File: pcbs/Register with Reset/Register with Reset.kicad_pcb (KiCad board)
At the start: 2 copper layers, 101.6 x 114.3 mm, 73 parts, among them J101 Conn_02x20_Odd_Even, U201 74HC245, U202 74HCT574, U203 74HC245, U301 74HC245, U302 74HCT574, U303 74HC245, U401 74HC08, U402 74HC14

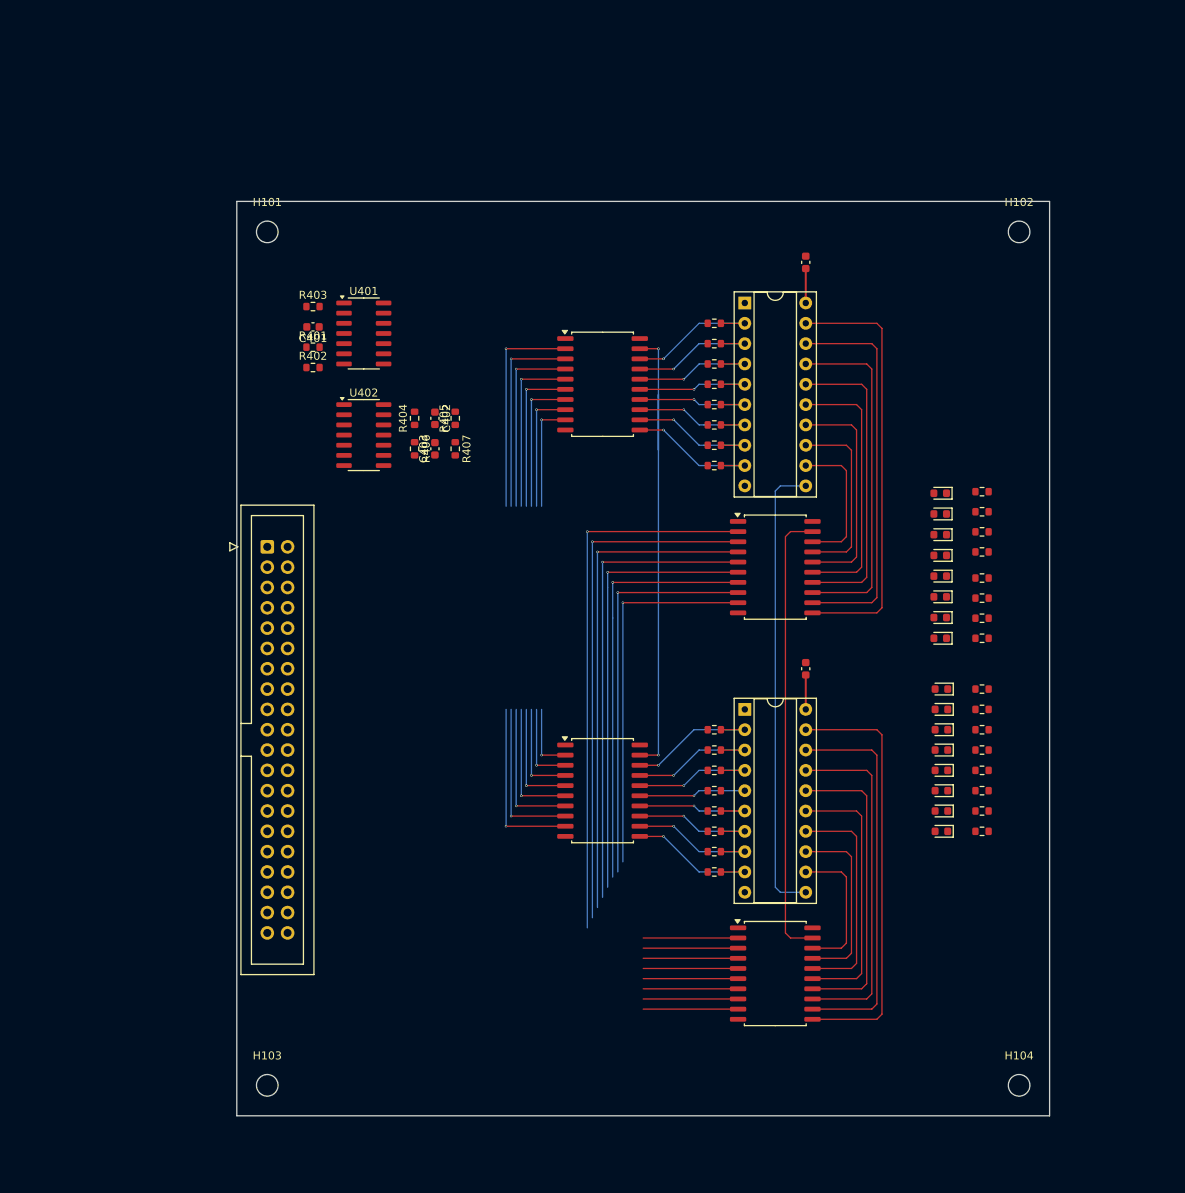
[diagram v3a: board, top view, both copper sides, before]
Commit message: First draft of whole board
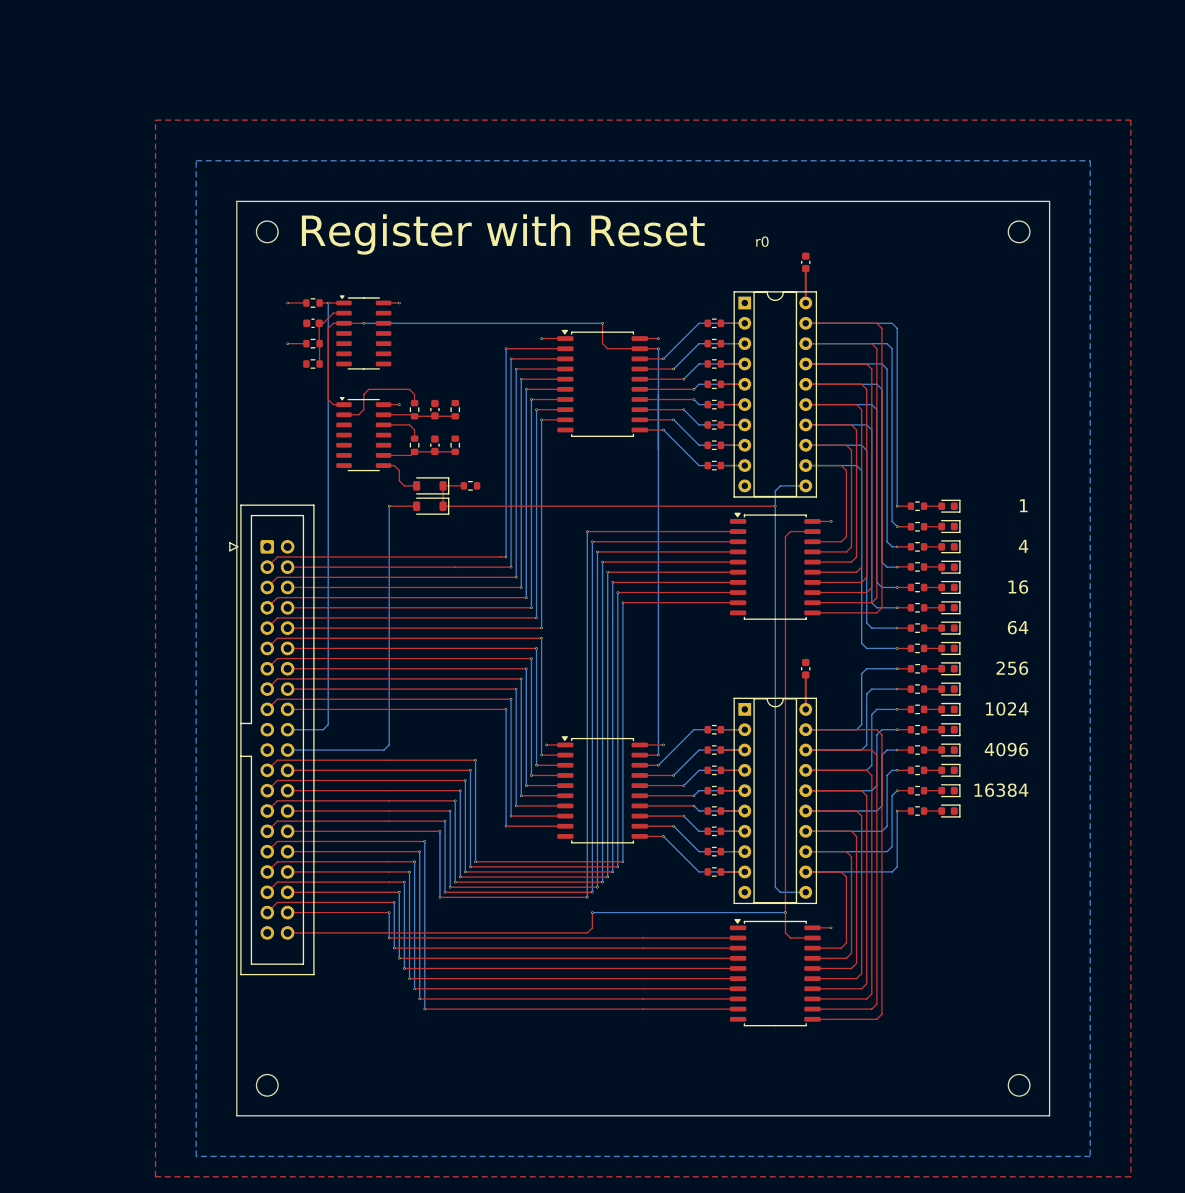
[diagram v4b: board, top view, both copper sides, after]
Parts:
- added D101: D, Diode_SMD:D_SOD-123, F.Cu at (87.6, 99.1)
- added D102: D, Diode_SMD:D_SOD-123, F.Cu at (87.6, 101.6)
- added R101: 1M, Resistor_SMD:R_0603_1608Metric, F.Cu at (92.7, 99.1)
- moved R312 8.46 mm to (148.6, 129.5)
- moved R316 8.46 mm to (148.6, 139.7)
- moved R310 8.46 mm to (148.6, 124.5)
- moved R309 8.46 mm to (148.6, 121.9)
- moved R311 8.46 mm to (148.6, 127.0)
- moved R313 8.46 mm to (148.6, 132.1)
- moved R314 8.46 mm to (148.6, 134.6)
- moved R315 8.46 mm to (148.6, 137.2)
- moved R210 8.28 mm to (148.6, 104.2)
- moved R211 8.28 mm to (148.6, 106.7)
- moved R212 8.28 mm to (148.6, 109.2)
- moved R209 8.27 mm to (148.6, 101.6)
- moved R216 8.16 mm to (148.6, 119.4)
- moved R215 8.16 mm to (148.6, 116.8)
- moved R214 8.16 mm to (148.6, 114.3)
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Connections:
- D201 pad 1: Net-(D201-K) -> GND
- D202 pad 1: Net-(D202-K) -> GND
- D203 pad 1: Net-(D203-K) -> GND
- D204 pad 1: Net-(D204-K) -> GND
- D205 pad 1: Net-(D205-K) -> GND
- D206 pad 1: Net-(D206-K) -> GND
- D207 pad 1: Net-(D207-K) -> GND
- D208 pad 1: Net-(D208-K) -> GND
- D301 pad 1: Net-(D301-K) -> GND
- D302 pad 1: Net-(D302-K) -> GND
- D303 pad 1: Net-(D303-K) -> GND
- D304 pad 1: Net-(D304-K) -> GND
- D305 pad 1: Net-(D305-K) -> GND
- D306 pad 1: Net-(D306-K) -> GND
- D307 pad 1: Net-(D307-K) -> GND
- D308 pad 1: Net-(D308-K) -> GND
- J101 pad 20: unconnected-(J101-Pin_20-Pad20) -> /~{RESET}
- J101 pad 22: unconnected-(J101-Pin_22-Pad22) -> /CLK
- J101 pad 40: unconnected-(J101-Pin_40-Pad40) -> /~{OE}
- R209 pad 1: Net-(D201-K) -> Net-(U202-Q0)
- R209 pad 2: GND -> Net-(D201-A)
- R210 pad 1: Net-(D202-K) -> Net-(U202-Q1)
- R210 pad 2: GND -> Net-(D202-A)
- R211 pad 1: Net-(D203-K) -> Net-(U202-Q2)
- R211 pad 2: GND -> Net-(D203-A)
- R212 pad 1: Net-(D204-K) -> Net-(U202-Q3)
- R212 pad 2: GND -> Net-(D204-A)
- R213 pad 1: Net-(D205-K) -> Net-(U202-Q4)
- R213 pad 2: GND -> Net-(D205-A)
- R214 pad 1: Net-(D206-K) -> Net-(U202-Q5)
- R214 pad 2: GND -> Net-(D206-A)
- R215 pad 1: Net-(D207-K) -> Net-(U202-Q6)
- R215 pad 2: GND -> Net-(D207-A)
- R216 pad 1: Net-(D208-K) -> Net-(U202-Q7)
- R216 pad 2: GND -> Net-(D208-A)
- R309 pad 1: Net-(D301-K) -> Net-(U302-Q0)
- R309 pad 2: GND -> Net-(D301-A)
- R310 pad 1: Net-(D302-K) -> Net-(U302-Q1)
- R310 pad 2: GND -> Net-(D302-A)
- R311 pad 1: Net-(D303-K) -> Net-(U302-Q2)
- R311 pad 2: GND -> Net-(D303-A)
- R312 pad 1: Net-(D304-K) -> Net-(U302-Q3)
- R312 pad 2: GND -> Net-(D304-A)
- R313 pad 1: Net-(D305-K) -> Net-(U302-Q4)
- R313 pad 2: GND -> Net-(D305-A)
- R314 pad 1: Net-(D306-K) -> Net-(U302-Q5)
- R314 pad 2: GND -> Net-(D306-A)
- R315 pad 1: Net-(D307-K) -> Net-(U302-Q6)
- R315 pad 2: GND -> Net-(D307-A)
- R316 pad 1: Net-(D308-K) -> Net-(U302-Q7)
- R316 pad 2: GND -> Net-(D308-A)
- R403 pad 2: /ResetLogic/~{RESET} -> /~{RESET}
- R404 pad 1: Net-(R404-Pad1) -> Net-(C402-Pad1)
- R404 pad 2: Net-(C402-Pad1) -> Net-(R404-Pad2)
- R405 pad 1: GND -> Net-(C402-Pad1)
- R405 pad 2: Net-(C402-Pad1) -> GND
- R406 pad 1: Net-(R406-Pad1) -> Net-(C403-Pad1)
- R406 pad 2: Net-(C403-Pad1) -> Net-(R406-Pad2)
- R407 pad 1: GND -> Net-(C403-Pad1)
- R407 pad 2: Net-(C403-Pad1) -> GND
- U202 pad 12: Net-(D208-A) -> Net-(U202-Q7)
- U202 pad 13: Net-(D207-A) -> Net-(U202-Q6)
- U202 pad 14: Net-(D206-A) -> Net-(U202-Q5)
- U202 pad 15: Net-(D205-A) -> Net-(U202-Q4)
- U202 pad 16: Net-(D204-A) -> Net-(U202-Q3)
- U202 pad 17: Net-(D203-A) -> Net-(U202-Q2)
- U202 pad 18: Net-(D202-A) -> Net-(U202-Q1)
- U202 pad 19: Net-(D201-A) -> Net-(U202-Q0)
- U203 pad 11: Net-(D201-A) -> Net-(U202-Q0)
- U203 pad 12: Net-(D202-A) -> Net-(U202-Q1)
- U203 pad 13: Net-(D203-A) -> Net-(U202-Q2)
- U203 pad 14: Net-(D204-A) -> Net-(U202-Q3)
- U203 pad 15: Net-(D205-A) -> Net-(U202-Q4)
- U203 pad 16: Net-(D206-A) -> Net-(U202-Q5)
- U203 pad 17: Net-(D207-A) -> Net-(U202-Q6)
- U203 pad 18: Net-(D208-A) -> Net-(U202-Q7)
- U203 pad 19: /Register 0/~{OE} -> /~{OE}
- U302 pad 12: Net-(D308-A) -> Net-(U302-Q7)
- U302 pad 13: Net-(D307-A) -> Net-(U302-Q6)
- U302 pad 14: Net-(D306-A) -> Net-(U302-Q5)
- U302 pad 15: Net-(D305-A) -> Net-(U302-Q4)
- U302 pad 16: Net-(D304-A) -> Net-(U302-Q3)
- U302 pad 17: Net-(D303-A) -> Net-(U302-Q2)
- U302 pad 18: Net-(D302-A) -> Net-(U302-Q1)
- U302 pad 19: Net-(D301-A) -> Net-(U302-Q0)
- U303 pad 11: Net-(D301-A) -> Net-(U302-Q0)
- U303 pad 12: Net-(D302-A) -> Net-(U302-Q1)
- U303 pad 13: Net-(D303-A) -> Net-(U302-Q2)
- U303 pad 14: Net-(D304-A) -> Net-(U302-Q3)
- U303 pad 15: Net-(D305-A) -> Net-(U302-Q4)
- U303 pad 16: Net-(D306-A) -> Net-(U302-Q5)
- U303 pad 17: Net-(D307-A) -> Net-(U302-Q6)
- U303 pad 18: Net-(D308-A) -> Net-(U302-Q7)
- U303 pad 19: /Register 0/~{OE} -> /~{OE}
- U401 pad 1: /ResetLogic/~{RESET} -> /~{RESET}
- U401 pad 10: unconnected-(U401-Pad10) -> GND
- U401 pad 12: unconnected-(U401-Pad12) -> GND
- U401 pad 13: unconnected-(U401-Pad13) -> GND
- U401 pad 3: /ResetLogic/~{ZeroInput} -> /Register 0/~{ZeroInput}
- U401 pad 4: unconnected-(U401-Pad4) -> GND
- U401 pad 5: unconnected-(U401-Pad5) -> GND
- U401 pad 9: unconnected-(U401-Pad9) -> GND
- U402 pad 1: /ResetLogic/~{ZeroInput} -> /Register 0/~{ZeroInput}
- U402 pad 11: unconnected-(U402-Pad11) -> GND
- U402 pad 12: Net-(R406-Pad1) -> Net-(R406-Pad2)
- U402 pad 2: Net-(R404-Pad1) -> Net-(R404-Pad2)
- U402 pad 3: unconnected-(U402-Pad3) -> GND
- U402 pad 5: unconnected-(U402-Pad5) -> GND
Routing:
- net /~{OE}: track 0.00 -> 121.2 mm, vias 0 -> 2
- net Net-(U202-Q0): track 0.00 -> 89.3 mm, vias 0 -> 1
- net Net-(U202-Q1): track 0.00 -> 83.9 mm, vias 0 -> 1
- net Net-(U202-Q2): track 0.00 -> 78.8 mm, vias 0 -> 1
- net Net-(U202-Q3): track 0.00 -> 73.7 mm, vias 0 -> 1
- net Net-(U302-Q0): track 0.00 -> 73.7 mm, vias 0 -> 1
- net Net-(U302-Q1): track 0.00 -> 68.6 mm, vias 0 -> 1
- net Net-(U202-Q4): track 0.00 -> 68.6 mm, vias 0 -> 1
- net /Reg1.Out0: track 11.9 -> 80.3 mm, vias 0 -> 2
- net Net-(U302-Q2): track 0.00 -> 63.5 mm, vias 0 -> 1
- net Net-(U202-Q5): track 0.00 -> 63.5 mm, vias 0 -> 1
- net /Reg1.Out2: track 11.9 -> 75.3 mm, vias 0 -> 2
- net /Reg1.Out1: track 11.9 -> 74.7 mm, vias 0 -> 2
- net /~{RESET}: track 0.00 -> 61.1 mm, vias 0 -> 1
- net Net-(U302-Q3): track 0.00 -> 58.4 mm, vias 0 -> 1
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- added copper zone on B.Cu, net +5V
- added copper zone on F.Cu, net GND
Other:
- board text added: "${TITLE}"
- board text added: "1"
- board text added: "1024"
- board text added: "16"
- board text added: "16384"
- board text added: "256"
- board text added: "4"
- board text added: "4096"
- board text added: "64"
- board text added: "r${REVISION}"

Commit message: Add order number mark
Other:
- board text added: "JLCJLCJLCJLC"
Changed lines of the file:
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@@
 		(tags "SOD-123")
 		(property "Reference" "D102"
-			(at 0 -2 360)
+			(at 0 -2 0)
 			(layer "F.SilkS")
 			(hide yes)
@@
 		)
 		(property "Value" "D"
-			(at 0 2.1 360)
+			(at 0 2.1 0)
 			(layer "F.Fab")
 			(effects
@@
 		)
 		(fp_text user "${REFERENCE}"
-			(at 0 -2 360)
+			(at 0 -2 0)
 			(layer "F.Fab")
 			(effects
@@
 		(tags "SOD-123")
 		(property "Reference" "D101"
-			(at 0 -2 360)
+			(at 0 -2 0)
 			(layer "F.SilkS")
 			(hide yes)
@@
 		)
 		(property "Value" "D"
-			(at 0 2.1 360)
+			(at 0 2.1 0)
 			(layer "F.Fab")
 			(effects
@@
 		)
 		(fp_text user "${REFERENCE}"
-			(at 0 -2 360)
+			(at 0 -2 0)
 			(layer "F.Fab")
 			(effects
@@
 		(tags "resistor")
 		(property "Reference" "R101"
-			(at 0 -1.43 360)
+			(at 0 -1.43 0)
 			(layer "F.SilkS")
 			(hide yes)
@@
 		)
 		(property "Value" "1M"
-			(at 0 1.43 360)
+			(at 0 1.43 0)
 			(layer "F.Fab")
 			(effects
@@
 		)
 		(fp_text user "${REFERENCE}"
-			(at 0 0 360)
+			(at 0 0 0)
 			(layer "F.Fab")
 			(effects
@@
 		(layer "Edge.Cuts")
 	)
+	(gr_text "JLCJLCJLCJLC"
+		(at 81.28 173.99 0)
+		(layer "B.SilkS")
+		(effects
+			(font
+				(size 1 1)
+				(thickness 0.1)
+			)
+			(justify left mirror)
+		)
+	)
 	(gr_text "64"

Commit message: Fix the reset logic....
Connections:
- U201 pad 19: /Register 0/~{ZeroInput} -> /Register 0/ZeroInput
- U301 pad 19: /Register 0/~{ZeroInput} -> /Register 0/ZeroInput
- U401 pad 3: /Register 0/~{ZeroInput} -> Net-(U401-Pad3)
- U402 pad 1: /Register 0/~{ZeroInput} -> Net-(U401-Pad3)
- U402 pad 3: GND -> Net-(U401-Pad3)
- U402 pad 4: unconnected-(U402-Pad4) -> /Register 0/ZeroInput
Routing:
- net /Register 0/~{ZeroInput}: track 122.6 -> 0.00 mm, vias 4 -> 0
- net /Register 0/ZeroInput: track 0.00 -> 111.2 mm, vias 0 -> 3
- net Net-(U401-Pad3): track 0.00 -> 20.1 mm
- net Net-(R404-Pad2): track 12.6 -> 13.3 mm, vias 0 -> 2
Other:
- board text added: "0"
- board text added: "10"
- board text added: "12"
- board text added: "14"
- board text added: "2"
- board text added: "6"
- board text added: "8"
- board text removed: "1"
- board text removed: "1024"
- board text removed: "16"
- board text removed: "16384"
- board text removed: "256"
- board text removed: "4096"
- board text removed: "64"
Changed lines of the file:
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@@
 	(net 36 "Net-(U301-B3)")
 	(net 37 "Net-(U301-B7)")
-	(net 38 "/Register 0/~{ZeroInput}")
+	(net 38 "/Register 0/ZeroInput")
 	(net 39 "/Register 0/RegClk")
 	(net 40 "Net-(C401-Pad1)")
@@
 	(net 57 "Net-(U202-Q4)")
 	(net 58 "unconnected-(U402-Pad6)")
-	(net 59 "unconnected-(U402-Pad4)")
+	(net 59 "Net-(U401-Pad3)")
 	(net 60 "Net-(U202-Q5)")
 	(net 61 "/Reg1.In7")
@@
 			(layers "F.Cu" "F.Paste" "F.Mask")
 			(roundrect_rratio 0.25)
-			(net 38 "/Register 0/~{ZeroInput}")
+			(net 38 "/Register 0/ZeroInput")
 			(pinfunction "CE")
 			(pintype "input")
@@
 			(layers "F.Cu" "F.Paste" "F.Mask")
 			(roundrect_rratio 0.25)
-			(net 38 "/Register 0/~{ZeroInput}")
+			(net 38 "/Register 0/ZeroInput")
 			(pinfunction "CE")
 			(pintype "input")
@@
 			(layers "F.Cu" "F.Paste" "F.Mask")
 			(roundrect_rratio 0.25)
-			(net 38 "/Register 0/~{ZeroInput}")
+			(net 59 "Net-(U401-Pad3)")
 			(pintype "input")
 		)
@@
 			(layers "F.Cu" "F.Paste" "F.Mask")
 			(roundrect_rratio 0.25)
-			(net 21 "GND")
+			(net 59 "Net-(U401-Pad3)")
 			(pintype "input")
 		)
@@
 			(layers "F.Cu" "F.Paste" "F.Mask")
 			(roundrect_rratio 0.25)
-			(net 59 "unconnected-(U402-Pad4)")
-			(pintype "output+no_connect")
+			(net 38 "/Register 0/ZeroInput")
+			(pintype "output")
 		)
 		(pad "5" smd roundrect
@@
 			(layers "F.Cu" "F.Paste" "F.Mask")
 			(roundrect_rratio 0.25)
-			(net 38 "/Register 0/~{ZeroInput}")
+			(net 59 "Net-(U401-Pad3)")
 			(pintype "output")
 		)
@@
 		)
 	)
-	(gr_text "64"
-		(at 162.56 116.84 0)
+	(gr_text "6"
+		(at 157.48 116.84 0)
 		(layer "F.SilkS")
 		(effects
@@
 		)
 	)
-	(gr_text "1"
-		(at 162.56 101.6 0)
+	(gr_text "0"
+		(at 157.48 101.6 0)
 		(layer "F.SilkS")
 		(effects
@@
 		)
 	)
-	(gr_text "16"
-		(at 162.56 111.76 0)
+	(gr_text "4"
+		(at 157.48 111.76 0)
 		(layer "F.SilkS")
 		(effects
@@
 		)
 	)
-	(gr_text "16384"
-		(at 162.56 137.16 0)
+	(gr_text "14"
+		(at 157.48 137.16 0)
 		(layer "F.SilkS")
 		(effects
@@
 		)
 	)
-	(gr_text "4096"
-		(at 162.56 132.08 0)
+	(gr_text "12"
+		(at 157.48 132.08 0)
 		(layer "F.SilkS")
 		(effects
@@
 		)
 	)
-	(gr_text "256"
-		(at 162.56 121.92 0)
+	(gr_text "8"
+		(at 157.48 121.92 0)
 		(layer "F.SilkS")
 		(effects
@@
 		)
 	)
-	(gr_text "4"
-		(at 162.56 106.68 0)
+	(gr_text "2"
+		(at 157.48 106.68 0)
 		(layer "F.SilkS")
 		(effects
@@
 		)
 	)
-	(gr_text "1024"
-		(at 162.56 127 0)
+	(gr_text "10"
+		(at 157.48 127 0)
 		(layer "F.SilkS")
 		(effects
@@
 	)
 	(segment
-		(start 75.565 78.74)
-		(end 74.93 79.375)
-		(width 0.127)
-		(layer "F.Cu")
-		(net 38)
-	)
-	(segment
-		(start 113.87 81.915)
-		(end 109.855 81.915)
+		(start 116.205 95.885)
+		(end 80.01 95.885)
 		(width 0.127)
 		(layer "F.Cu")
@@
 	)
 	(segment
-		(start 76.9 78.74)
-		(end 79.375 78.74)
-		(width 0.127)
-		(layer "F.Cu")
-		(net 38)
-	)
-	(segment
-		(start 113.87 81.915)
-		(end 116.205 81.915)
-		(width 0.127)
-		(layer "F.Cu")
-		(net 38)
-	)
-	(segment
-		(start 109.22 81.28)
-		(end 109.22 78.74)
+		(start 78.74 92.71)
+		(end 76.9 92.71)
 		(width 0.127)
 		(layer "F.Cu")
@@
 	)
 	(segment
-		(start 74.93 88.265)
-		(end 75.565 88.9)
-		(width 0.127)
-		(layer "F.Cu")
-		(net 38)
-	)
-	(segment
-		(start 76.9 78.74)
-		(end 75.565 78.74)
+		(start 78.74 92.71)
+		(end 79.375 93.345)
 		(width 0.127)
 		(layer "F.Cu")
@@
 	)
 	(segment
-		(start 74.93 79.375)
-		(end 74.93 88.265)
+		(start 79.375 95.25)
+		(end 79.375 93.345)
 		(width 0.127)
 		(layer "F.Cu")
@@
 	)
 	(segment
-		(start 109.855 81.915)
-		(end 109.22 81.28)
+		(start 80.01 95.885)
+		(end 79.375 95.25)
 		(width 0.127)
 		(layer "F.Cu")
@@
 	)
 	(segment
-		(start 75.565 88.9)
-		(end 76.9 88.9)
+		(start 113.87 81.915)
+		(end 116.205 81.915)
 		(width 0.127)
 		(layer "F.Cu")
@@
 	)
 	(via
-		(at 109.22 78.74)
-		(size 0.3)
-		(drill 0.2)
-		(layers "F.Cu" "B.Cu")
-		(net 38)
-	)
-	(via
 		(at 116.205 132.715)
 		(size 0.3)
@@
 	)
 	(via
-		(at 79.375 78.74)
+		(at 116.205 95.885)
 		(size 0.3)
 		(drill 0.2)
@@
 	)
 	(segment
-		(start 79.375 78.74)
-		(end 109.22 78.74)
+		(start 116.205 95.885)
+		(end 116.205 132.715)
 		(width 0.127)
 		(layer "B.Cu")
@@
 	(segment
 		(start 116.205 87.63)
-		(end 116.205 132.715)
+		(end 116.205 95.885)
 		(width 0.127)
 		(layer "B.Cu")
@@
 	)
 	(segment
-		(start 80.01 86.995)
-		(end 85.09 86.995)
-		(width 0.127)
-		(layer "F.Cu")
-		(net 43)
-	)
-	(segment
-		(start 78.74 90.17)
-		(end 79.375 89.535)
+		(start 85.09 86.995)
+		(end 85.725 87.63)
 		(width 0.127)
 		(layer "F.Cu")
@@
 	)
 	(segment
-		(start 79.375 87.63)
-		(end 80.01 86.995)
+		(start 85.725 87.63)
+		(end 85.725 88.71)
 		(width 0.127)
 		(layer "F.Cu")
@@
 	)
 	(segment
-		(start 85.725 87.63)
-		(end 85.725 88.71)
+		(start 78.74 86.995)
+		(end 85.09 86.995)
 		(width 0.127)
 		(layer "F.Cu")
@@
 		(net 43)
 	)
-	(segment
-		(start 79.375 89.535)
-		(end 79.375 87.63)
-		(width 0.127)
-		(layer "F.Cu")
+	(via
+		(at 78.74 90.17)
+		(size 0.3)
+		(drill 0.2)
+		(layers "F.Cu" "B.Cu")
+		(net 43)
+	)
+	(via
+		(at 78.74 86.995)
+		(size 0.3)
+		(drill 0.2)
+		(layers "F.Cu" "B.Cu")
 		(net 43)
 	)
 	(segment
-		(start 85.09 86.995)
-		(end 85.725 87.63)
+		(start 78.74 90.17)
+		(end 78.74 86.995)
 		(width 0.127)
-		(layer "F.Cu")
+		(layer "B.Cu")
 		(net 43)
 	)
@@
 	)
 	(segment
+		(start 75.565 78.74)
+		(end 74.93 79.375)
+		(width 0.127)
+		(layer "F.Cu")
+		(net 59)
+	)
+	(segment
+		(start 79.375 90.805)
+		(end 78.74 91.44)
+		(width 0.127)
+		(layer "F.Cu")
+		(net 59)
+	)
+	(segment
+		(start 76.9 88.9)
+		(end 78.74 88.9)
+		(width 0.127)
+		(layer "F.Cu")
+		(net 59)
+	)
+	(segment
+		(start 74.93 88.265)
+		(end 75.565 88.9)
+		(width 0.127)
+		(layer "F.Cu")
+		(net 59)
+	)
+	(segment
+		(start 76.9 78.74)
+		(end 75.565 78.74)
+		(width 0.127)
+		(layer "F.Cu")
+		(net 59)
+	)
+	(segment
+		(start 78.74 88.9)
+		(end 79.375 89.535)
+		(width 0.127)
+		(layer "F.Cu")
+		(net 59)
+	)
+	(segment
+		(start 74.93 79.375)
+		(end 74.93 88.265)
+		(width 0.127)
+		(layer "F.Cu")
+		(net 59)
+	)
+	(segment
+		(start 75.565 88.9)
+		(end 76.9 88.9)
+		(width 0.127)
+		(layer "F.Cu")
+		(net 59)
+	)
+	(segment
+		(start 78.74 91.44)
+		(end 76.9 91.44)
+		(width 0.127)
+		(layer "F.Cu")
+		(net 59)
+	)
+	(segment
+		(start 79.375 89.535)
+		(end 79.375 90.805)
+		(width 0.127)
+		(layer "F.Cu")
+		(net 59)
+	)
+	(segment
